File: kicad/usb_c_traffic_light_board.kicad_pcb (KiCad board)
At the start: 2 copper layers, 57 x 14 mm, 0 parts

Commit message: 提交红绿灯控制板阶段性设计
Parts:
- added C1: 10uF, C_0805_2012Metric, F.Cu at (153.0, 122.5)
- added C2: 100nF, C_0603_1608Metric, F.Cu at (153.0, 119.0)
- added C3: 100nF, C_0603_1608Metric, F.Cu at (144.0, 119.0)
- added D1: 绿灯, LED_1206_3216Metric, F.Cu at (148.5, 83.5)
- added D2: 橙灯, LED_1206_3216Metric, F.Cu at (148.5, 105.5)
- added D3: 红灯, LED_1206_3216Metric, F.Cu at (148.5, 126.5)
- added J1: 背面立式USB-C, USB_C_Receptacle_G-Switch_GT-USB-7051x, B.Cu at (148.5, 97.5)
- added R1: 1k, R_0603_1608Metric, F.Cu at (152.5, 126.5)
- added R2: 1k, R_0603_1608Metric, F.Cu at (152.5, 105.5)
- added R3: 1k, R_0603_1608Metric, F.Cu at (152.5, 83.5)
- added R4: 22R, R_0603_1608Metric, F.Cu at (143.9, 111.0)
- added R5: 22R, R_0603_1608Metric, F.Cu at (145.4, 111.0)
- added R6: 5.1k, R_0603_1608Metric, F.Cu at (151.7, 111.0)
- added R7: 5.1k, R_0603_1608Metric, F.Cu at (153.3, 111.0)
- added U1: CH552G, SOIC-16_3.9x9.9mm_P1.27mm, F.Cu at (148.5, 115.5)
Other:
- board size 57 x 14 mm -> 14 x 57 mm
- rule pad_to_mask_clearance: 0.05 -> 0
- board text added: "A2"
- board text added: "TP"
- board text removed: "USB-C 端"
- board text removed: "红灯"
- board text removed: "绿灯"
- board text removed: "黄灯"

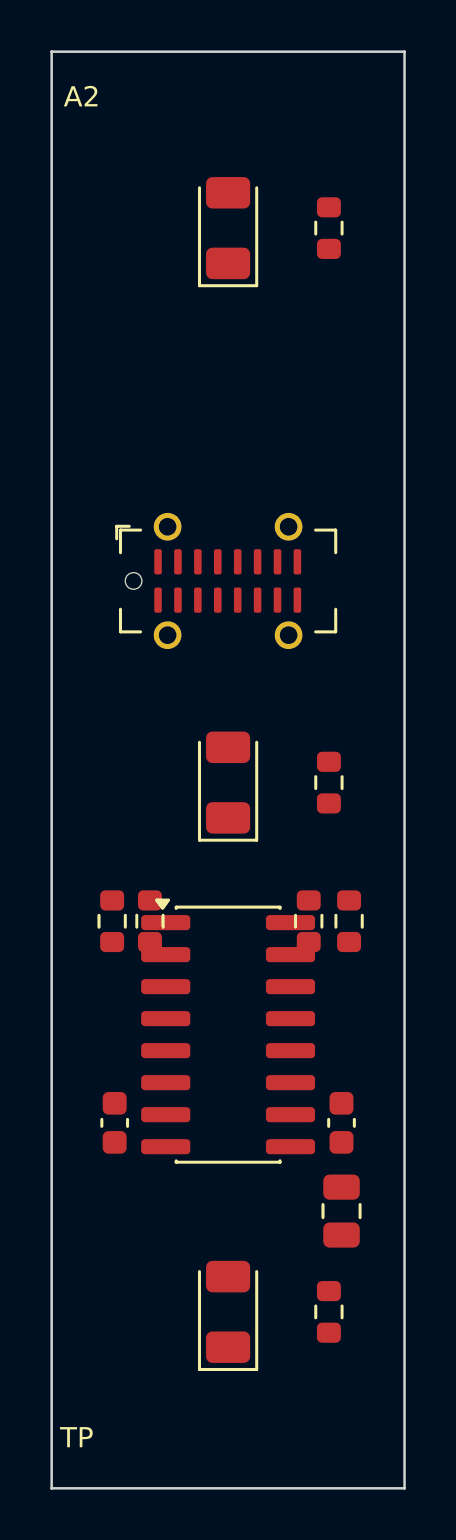
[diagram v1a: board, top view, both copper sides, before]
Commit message: 完成红绿灯控制板布线
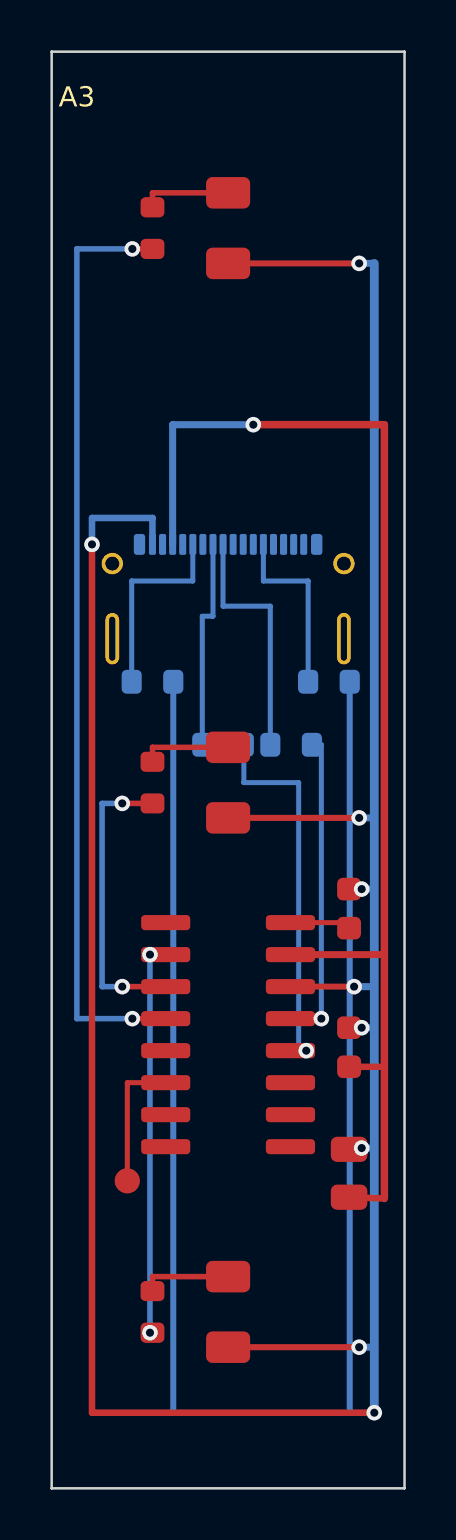
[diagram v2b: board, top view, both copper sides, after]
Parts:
- added TP1: RST, TestPoint_Pad_D1.0mm, F.Cu at (144.5, 121.3)
- J1: value 背面立式USB-C -> 背面USB-C; footprint USB_C_Receptacle_G-Switch_GT-USB-7051x -> USB_C_Receptacle_G-Switch_GT-USB-7025
- R4, R5, R6, R7: moved to B.Cu
- moved C3 12.6 mm to (153.3, 110.5)
- moved R6 11.3 mm to (145.5, 101.5), turned to 0 degrees
- moved R7 9.53 mm to (152.5, 101.5), turned to 0 degrees
- moved R5 8.96 mm to (151.0, 104.0), turned to 0 degrees
- moved R4 8.27 mm to (148.3, 104.0), turned to 0 degrees
- moved R1 7.00 mm to (145.5, 126.5)
- moved R2 7.00 mm to (145.5, 105.5)
- moved R3 7.00 mm to (145.5, 83.5)
- moved C2 3.01 mm to (153.3, 116.0)
- moved J1 2.00 mm to (148.5, 99.5)
- moved C1 1.53 mm to (153.3, 121.0)
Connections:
- J1 pad A12: GND -> (no net)
- J1 pad A9: 5V -> (no net)
- J1 pad B1: GND -> (no net)
- J1 pad B12: GND -> (no net)
- J1 pad B4: 5V -> (no net)
- J1 pad B6: USB_D+_CONN -> (no net)
- J1 pad B7: USB_D-_CONN -> (no net)
- J1 pad B9: 5V -> (no net)
- J1 pad SH: GND -> (no net)
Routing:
- net GND: track 0.00 -> 186.4 mm, vias 0 -> 9
- net 5V: track 0.00 -> 50.4 mm, vias 0 -> 1
- net LED_G: track 0.00 -> 37.1 mm, vias 0 -> 2
- net LED_R: track 0.00 -> 15.7 mm, vias 0 -> 2
- net USB_D+: track 0.00 -> 15.2 mm, vias 0 -> 1
- net USB_D-: track 0.00 -> 12.5 mm, vias 0 -> 1
- net LED_Y: track 0.00 -> 11.8 mm, vias 0 -> 2
- net USB_D-_CONN: track 0.00 -> 9.83 mm
- net USB_D+_CONN: track 0.00 -> 8.38 mm
- net CC1: track 0.00 -> 7.87 mm
- net CC2: track 0.00 -> 7.23 mm
- net RST: track 0.00 -> 5.42 mm
- net LED_Y_A: track 0.00 -> 3.58 mm
- net LED_R_A: track 0.00 -> 3.58 mm
- net LED_G_A: track 0.00 -> 3.58 mm
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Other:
- board text added: "A3"
- board text removed: "A2"
- board text removed: "TP"

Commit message: 完善机械轮廓和测量记录
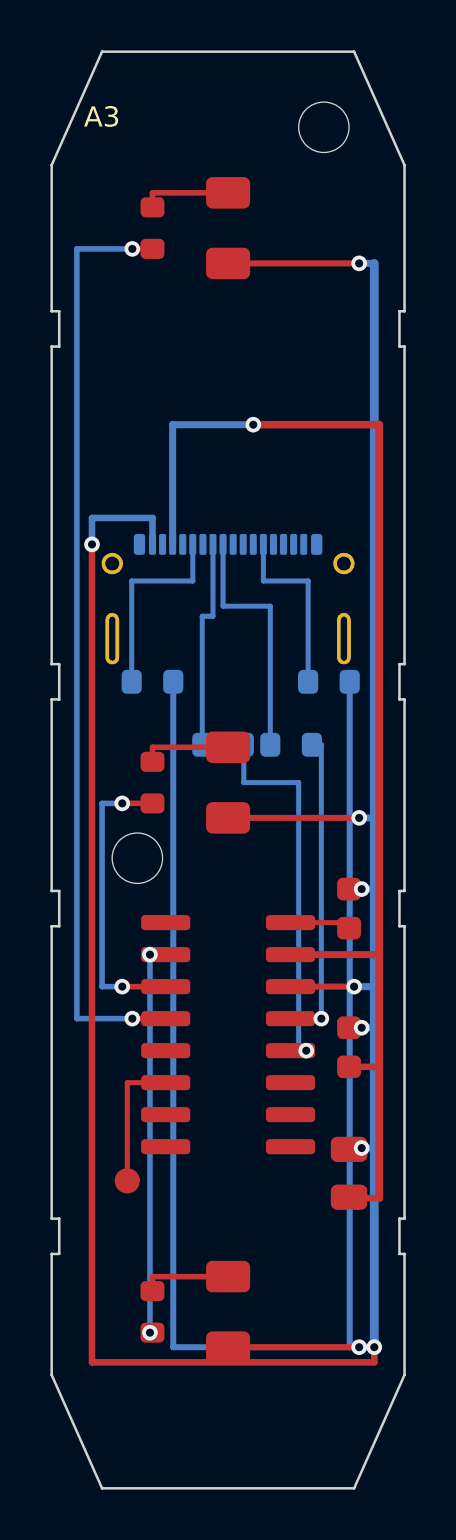
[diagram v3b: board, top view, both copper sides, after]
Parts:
- added H1: 上螺丝孔, MountingHole_2mm, F.Cu at (152.3, 79.5)
- added H2: 下螺丝孔, MountingHole_2mm, F.Cu at (144.9, 108.5)
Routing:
- net GND: track 186.4 -> 177.2 mm
- net 5V: track 50.4 -> 49.6 mm
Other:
- outline, holes or cut-outs redrawn

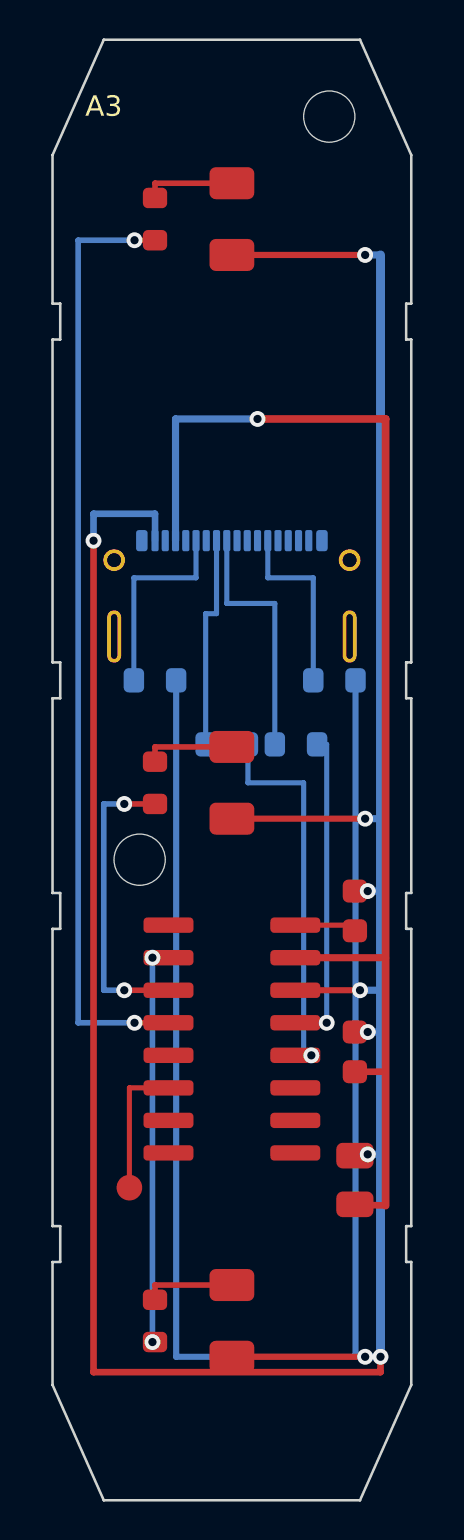
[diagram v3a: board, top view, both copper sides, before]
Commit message: 避位槽的深度不够，仍需修改
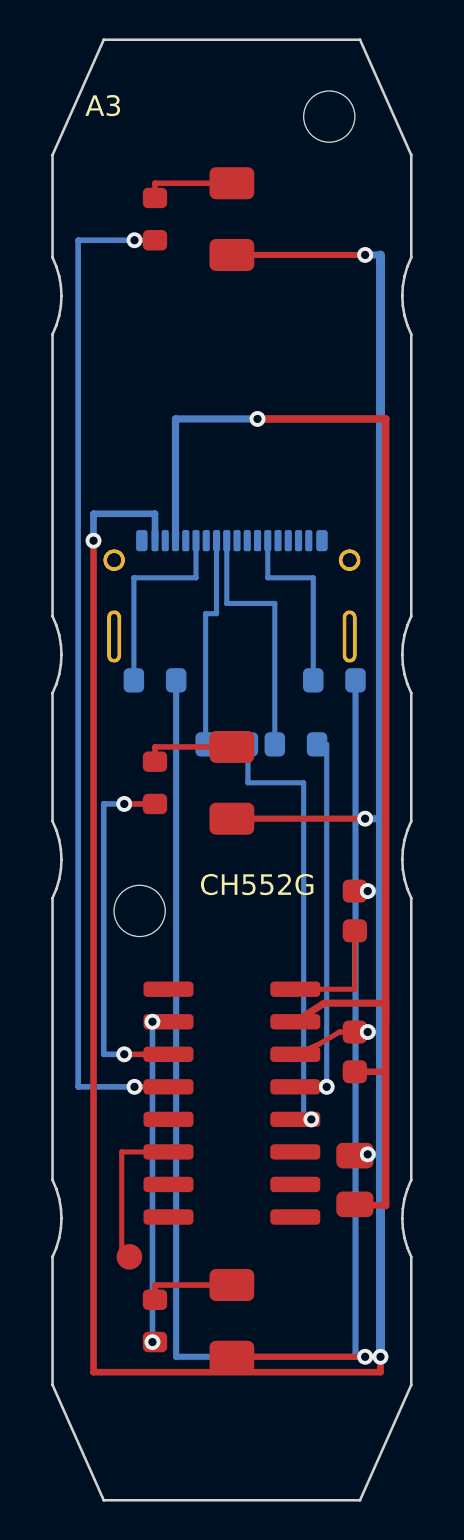
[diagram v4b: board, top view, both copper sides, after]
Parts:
- moved TP1 2.70 mm to (144.5, 124.0)
- moved U1 2.50 mm to (148.5, 118.0)
- moved H2 2.00 mm to (144.9, 110.5)
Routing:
- net USB_D-: track 12.5 -> 15.0 mm
- net USB_D+: track 15.2 -> 17.7 mm
- net LED_Y: track 11.8 -> 14.3 mm
- net LED_R: track 15.7 -> 13.2 mm
- net LED_G: track 37.1 -> 39.6 mm
- net V33: track 2.55 -> 4.61 mm
- net 5V: track 49.6 -> 50.5 mm
- net RST: track 5.42 -> 6.22 mm
- net GND: track 177.2 -> 176.4 mm, vias 9 -> 8
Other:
- outline, holes or cut-outs redrawn
- board text added: "CH552G"
